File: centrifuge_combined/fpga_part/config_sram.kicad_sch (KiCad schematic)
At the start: 5 parts, among them U1 XC7A100T-FTG256, U2 S25FL127SABMFV10, U3 CY7C1370KV33

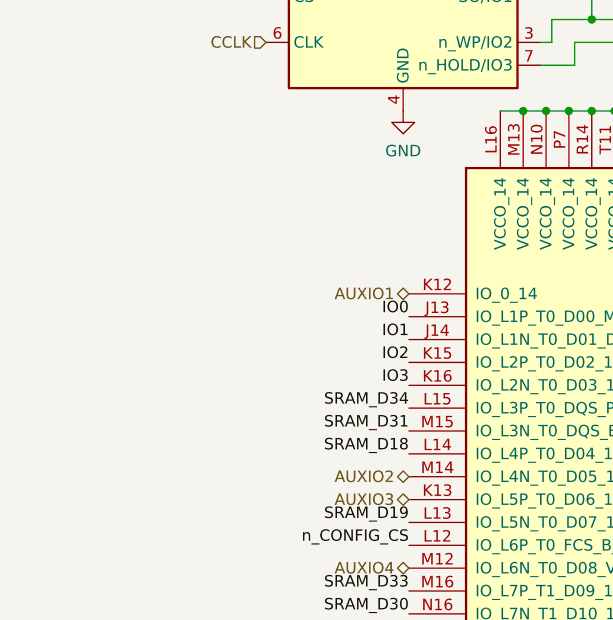
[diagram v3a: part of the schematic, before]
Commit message: Fixed Elprint complaints and JTAG VREF problems+config flash CS
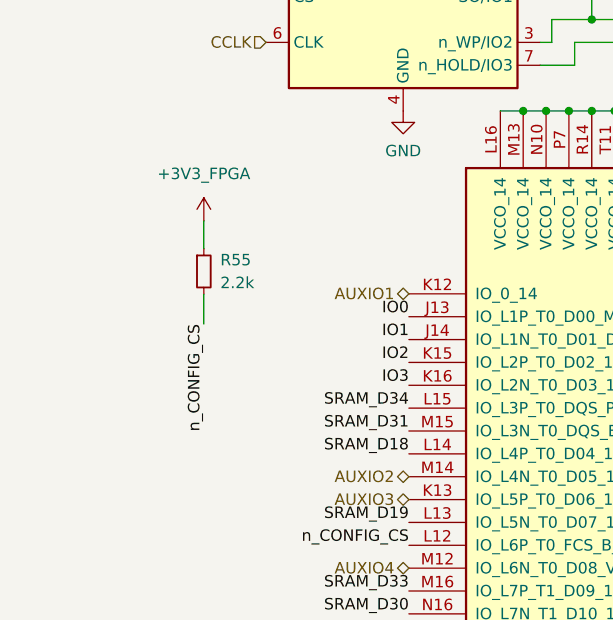
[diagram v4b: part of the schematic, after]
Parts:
- added R55: 2.2k, Resistor_SMD:R_0805_2012Metric_Pad1.20x1.40mm_HandSolder, symbol Device:R_Small
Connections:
- net +3V3_FPGA: now also R55.1
- net n_CONFIG_CS: now also R55.2
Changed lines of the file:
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@@
   (title_block
     (title "VGA Centrifuge")
-    (date "2022-10-03")
-    (rev "R3")
+    (date "2022-10-05")
+    (rev "R4")
     (comment 1 "Author: Paolo Celati")
     (comment 2 "FPGA Configuration Flash & SRAM")
@@
     (stroke (width 0) (type default) (color 0 0 0 0))
   )
+  (wire (pts (xy 26.1112 56.007) (xy 26.1112 59.1058))
+    (stroke (width 0) (type default) (color 0 0 0 0))
+  )
   (wire (pts (xy 180.975 99.06) (xy 164.465 99.06))
     (stroke (width 0) (type default) (color 0 0 0 0))
@@
   )
   (wire (pts (xy 117.475 28.575) (xy 120.015 28.575))
+    (stroke (width 0) (type default) (color 0 0 0 0))
+  )
+  (wire (pts (xy 26.1112 64.1858) (xy 26.1112 67.4878))
     (stroke (width 0) (type default) (color 0 0 0 0))
   )
@@
   (label "SRAM_A9" (at 150.495 104.775 0)
     (effects (font (size 1.27 1.27)) (justify left bottom))
+  )
+  (label "n_CONFIG_CS" (at 26.1112 67.4878 270)
+    (effects (font (size 1.27 1.27)) (justify right bottom))
   )
   (label "SRAM_D7" (at 150.495 140.335 0)
@@
     (pin "1")
   )
+  (symbol (lib_id "centrifuge_symbols:+3V3_FPGA") (at 26.1112 56.007 0) (unit 1)
+    (in_bom yes) (on_board yes) (fields_autoplaced)
+    (property "Reference" "#PWR0222" (id 0) (at 26.1112 59.817 0)
+      (effects (font (size 1.27 1.27)) hide)
+    )
+    (property "Value" "+3V3_FPGA" (id 1) (at 26.1112 50.8 0))
+    (property "Footprint" "" (id 2) (at 26.1112 56.007 0)
+      (effects (font (size 1.27 1.27)) hide)
+    )
+    (property "Datasheet" "" (id 3) (at 26.1112 56.007 0)
+      (effects (font (size 1.27 1.27)) hide)
+    )
+    (pin "1")
+  )
+  (symbol (lib_id "Device:R_Small") (at 26.1112 61.6458 0) (unit 1)
+    (in_bom yes) (on_board yes)
+    (property "Reference" "R55" (id 0) (at 27.94 60.3757 0)
+      (effects (font (size 1.27 1.27)) (justify left))
+    )
+    (property "Value" "2.2k" (id 1) (at 27.94 62.9157 0)
+      (effects (font (size 1.27 1.27)) (justify left))
+    )
+    (property "Footprint" "Resistor_SMD:R_0805_2012Metric_Pad1.20x1.40mm_HandSolder" (id 2) (at 26.1112 61.6458 0)
+      (effects (font (size 1.27 1.27)) hide)
+    )
+    (property "Datasheet" "~" (id 3) (at 26.1112 61.6458 0)
+      (effects (font (size 1.27 1.27)) hide)
+    )
+    (property "Order Page" "https://no.mouser.com/ProductDetail/Vishay-Dale/CRCW08052K20FKEB?qs=sGAEpiMZZMtlubZbdhIBINvvmcV35a3LmL3hFYkil7g%3D" (id 4) (at 26.1112 61.6458 0)
+      (effects (font (size 1.27 1.27)) hide)
+    )
+    (pin "1")
+    (pin "2")
+  )
   (symbol (lib_id "power:GND") (at 220.345 159.385 0) (unit 1)
